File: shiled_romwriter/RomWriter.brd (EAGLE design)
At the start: 68.6 x 53.3 mm, 13 parts, among them IC1 ATMEGA168-20P

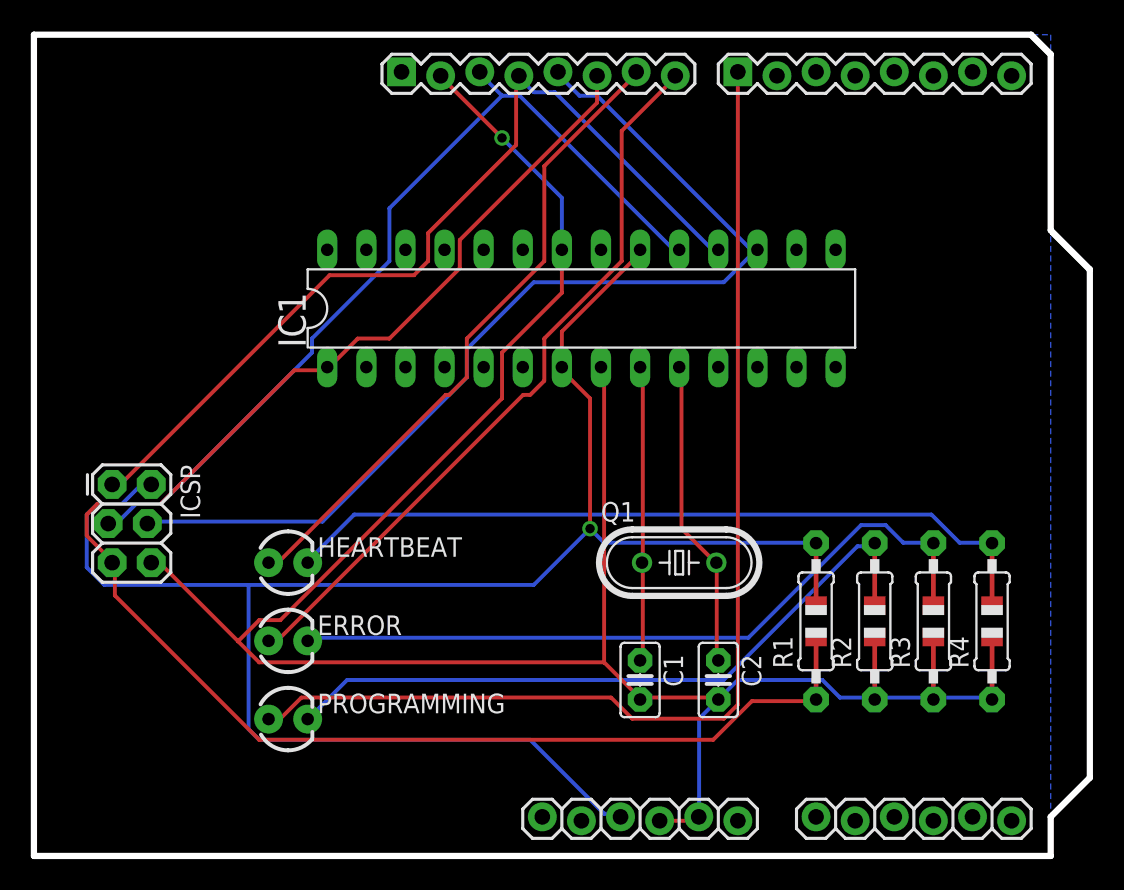
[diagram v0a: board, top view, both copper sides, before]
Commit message: Modified_shiled_romwriter
extra grounds update
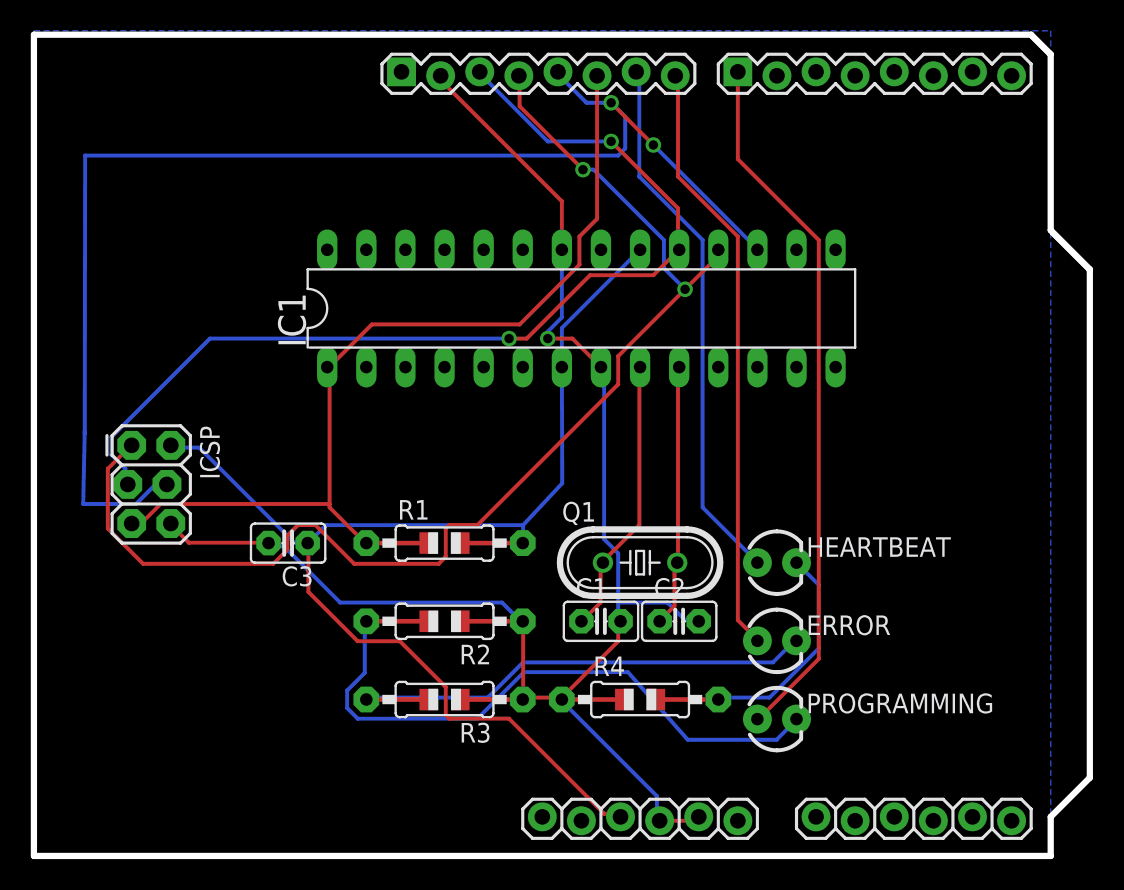
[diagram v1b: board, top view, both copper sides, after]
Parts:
- added C3: 0.1μF, capacitor-wima:C2.5-2
- R1: value (none) -> 10kΩ
- moved R3 32.2 mm to (26.7, 10.2), turned to 180 degrees
- moved ERROR 31.7 mm to (48.3, 14.0)
- moved HEARTBEAT 31.7 mm to (48.3, 19.1)
- moved PROGRAMMING 31.7 mm to (48.3, 8.89)
- moved R2 27.9 mm to (26.7, 15.2), turned to 180 degrees
- moved R1 24.7 mm to (26.7, 20.3), turned to 0 degrees
- moved R4 23.4 mm to (39.4, 10.2), turned to 0 degrees
- moved C2 4.58 mm to (41.9, 15.2), turned to 0 degrees
- moved C1 4.58 mm to (36.8, 15.2), turned to 0 degrees
- moved ICSP 2.84 mm to (6.35, 26.7)
- moved Q1 2.54 mm to (39.4, 19.1)
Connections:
- net +5V: now also C3.1
- net GND: now also C3.2
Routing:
- net RESET: track 103.7 -> 57.8 mm
- net GND: track 139.3 -> 100.9 mm
- net +5V: track 115.3 -> 78.8 mm, vias 1 -> 0
- net N$8: track 46.6 -> 14.1 mm
- net PGM_LED: track 73.1 -> 45.9 mm
- net MISO: track 58.7 -> 78.9 mm, vias 0 -> 2
- net MOSI: track 65.9 -> 85.3 mm, vias 0 -> 2
- net N$7: track 44.3 -> 29.5 mm
- net ERR_LED: track 48.3 -> 38.9 mm
- net SCK: track 57.4 -> 64.7 mm, vias 0 -> 2
- net HEART_LED: track 42.3 -> 35.1 mm
- net XTAL2: track 20.1 -> 17.0 mm
- net N$6: track 41.6 -> 39.4 mm
- net XTAL1: track 19.2 -> 18.1 mm
- added copper zone on layer 16, net GND
- removed copper zone on layer 16, net N$1
